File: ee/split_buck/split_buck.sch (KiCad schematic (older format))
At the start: 13 parts, among them J1 Conn_01x08, J3 Conn_01x03, Q1 DMP2160U

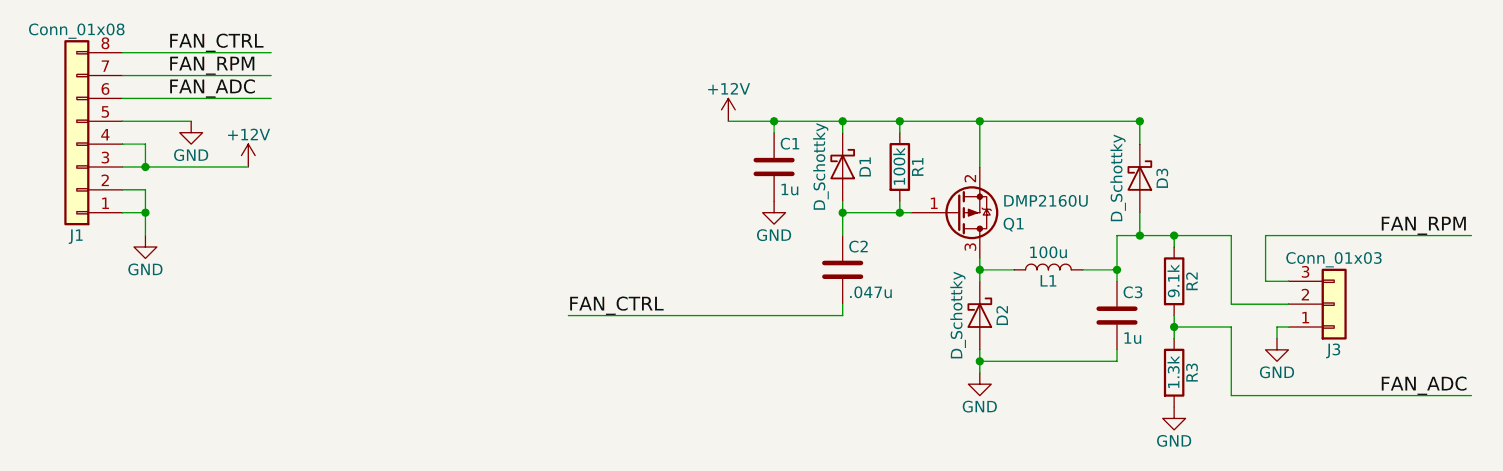
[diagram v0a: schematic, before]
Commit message: Update split_buck design
- switched D1 to zener to protect FET Vgs
- increased input/output caps from 1u to 10u (0603 -> 0805)
- rotated fan header 30degrees to enable multiple channels
- added net names
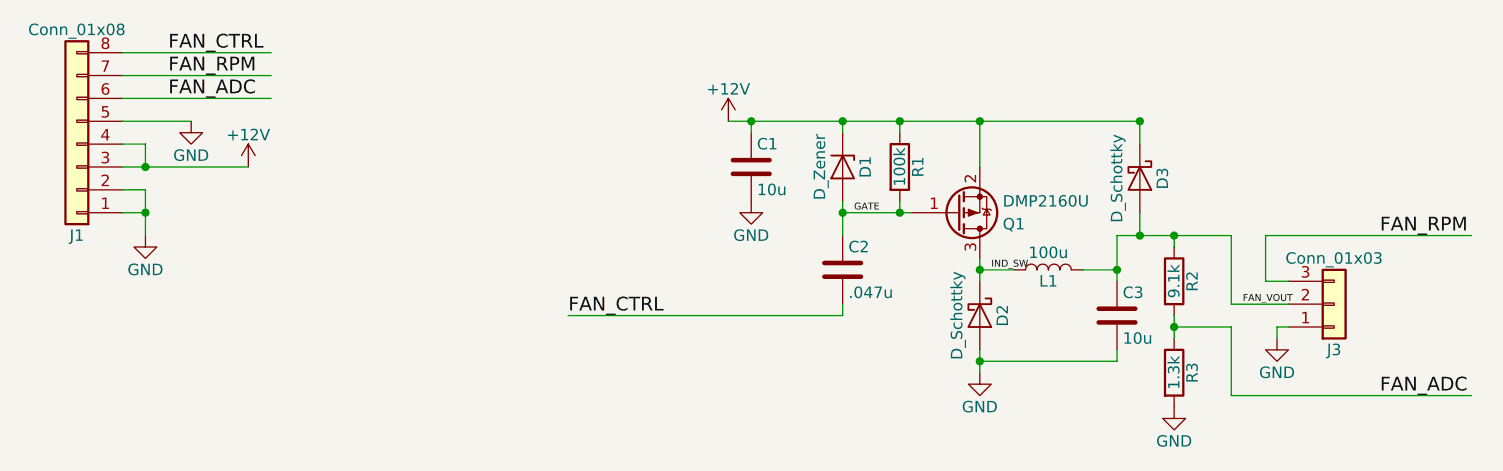
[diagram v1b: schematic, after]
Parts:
- removed D1: D_Schottky, Diodes_SMD:D_SOD-123, symbol D_Schottky
- added D1: D_Zener, Diodes_SMD:D_SOD-123, symbol D_Zener
- C1, C3: value 1u -> 10u; footprint Capacitors_SMD:C_0603_HandSoldering -> Capacitors_SMD:C_0805_HandSoldering
- L1: footprint Inductors_THT:L_Axial_L9.5mm_D4.0mm_P15.24mm_Horizontal_Fastron_SMCC -> Inductors_THT:L_Axial_L7.0mm_D3.3mm_P10.16mm_Horizontal_Fastron_MICC
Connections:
- net labels added: FAN_VOUT, GATE, IND_SW
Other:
- moved on the sheet: C1
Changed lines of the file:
@@
 LIBS:contrib
 LIBS:valves
+LIBS:joystick
 LIBS:stm32
 LIBS:w_connectors
-LIBS:joystick
-LIBS:vent_fan-cache
+LIBS:split_buck-cache
 EELAYER 25 0
 EELAYER END
@@
 F 0 "L1" V 5450 3400 50  0000 C CNN
 F 1 "100u" V 5575 3400 50  0000 C CNN
-F 2 "Inductors_THT:L_Axial_L9.5mm_D4.0mm_P15.24mm_Horizontal_Fastron_SMCC" H 5500 3400 50  0001 C CNN
+F 2 "Inductors_THT:L_Axial_L7.0mm_D3.3mm_P10.16mm_Horizontal_Fastron_MICC" H 5500 3400 50  0001 C CNN
 F 3 "" H 5500 3400 50  0001 C CNN
 	1    5500 3400
 	0    1    -1   0
-$EndComp
-$Comp
-L D_Schottky D1
-U 1 1 5AA40D58
-P 4600 2950
-F 0 "D1" H 4600 3050 50  0000 C CNN
-F 1 "D_Schottky" H 4600 2850 50  0000 C CNN
-F 2 "Diodes_SMD:D_SOD-123" H 4600 2950 50  0001 C CNN
-F 3 "" H 4600 2950 50  0001 C CNN
-	1    4600 2950
-	0    1    1    0
 $EndComp
 $Comp
@@
 L C C1
 U 1 1 5AA40F47
-P 4300 2950
-F 0 "C1" H 4325 3050 50  0000 L CNN
-F 1 "1u" H 4325 2850 50  0000 L CNN
-F 2 "Capacitors_SMD:C_0603_HandSoldering" H 4338 2800 50  0001 C CNN
-F 3 "" H 4300 2950 50  0001 C CNN
-	1    4300 2950
+P 4200 2950
+F 0 "C1" H 4225 3050 50  0000 L CNN
+F 1 "10u" H 4225 2850 50  0000 L CNN
+F 2 "Capacitors_SMD:C_0805_HandSoldering" H 4238 2800 50  0001 C CNN
+F 3 "" H 4200 2950 50  0001 C CNN
+	1    4200 2950
 	1    0    0    -1
 $EndComp
@@
 P 5800 3600
 F 0 "C3" H 5825 3700 50  0000 L CNN
-F 1 "1u" H 5825 3500 50  0000 L CNN
-F 2 "Capacitors_SMD:C_0603_HandSoldering" H 5838 3450 50  0001 C CNN
+F 1 "10u" H 5825 3500 50  0000 L CNN
+F 2 "Capacitors_SMD:C_0805_HandSoldering" H 5838 3450 50  0001 C CNN
 F 3 "" H 5800 3600 50  0001 C CNN
 	1    5800 3600
@@
 L GND #PWR03
 U 1 1 5AA416CE
-P 4300 3100
-F 0 "#PWR03" H 4300 2850 50  0001 C CNN
-F 1 "GND" H 4300 2950 50  0000 C CNN
-F 2 "" H 4300 3100 50  0001 C CNN
-F 3 "" H 4300 3100 50  0001 C CNN
-	1    4300 3100
+P 4200 3100
+F 0 "#PWR03" H 4200 2850 50  0001 C CNN
+F 1 "GND" H 4200 2950 50  0000 C CNN
+F 2 "" H 4200 3100 50  0001 C CNN
+F 3 "" H 4200 3100 50  0001 C CNN
+	1    4200 3100
 	1    0    0    -1
 $EndComp
@@
 Connection ~ 4850 3150
 Connection ~ 5200 3800
-Connection ~ 4300 2750
+Connection ~ 4200 2750
 Wire Wire Line
 	4100 2750 5900 2750
@@
 Connection ~ 4600 3150
 Wire Wire Line
-	4300 2750 4300 2800
+	4200 2750 4200 2800
 Wire Wire Line
 	4850 3100 4850 3150
@@
 	1550 2850 1550 2950
 Connection ~ 1550 2950
+$Comp
+L D_Zener D1
+U 1 1 5AAEA835
+P 4600 2950
+F 0 "D1" H 4600 3050 50  0000 C CNN
+F 1 "D_Zener" H 4600 2850 50  0000 C CNN
+F 2 "Diodes_SMD:D_SOD-123" H 4600 2950 50  0001 C CNN
+F 3 "" H 4600 2950 50  0001 C CNN
+	1    4600 2950
+	0    1    1    0
+$EndComp
+Text Label 6350 3550 0    30   ~ 0
+FAN_VOUT
+Text Label 4650 3150 0    30   ~ 0
+GATE
+Text Label 5250 3400 0    30   ~ 0
+IND_SW
 $EndSCHEMATC

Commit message: update layout for carrier with new pin assignments
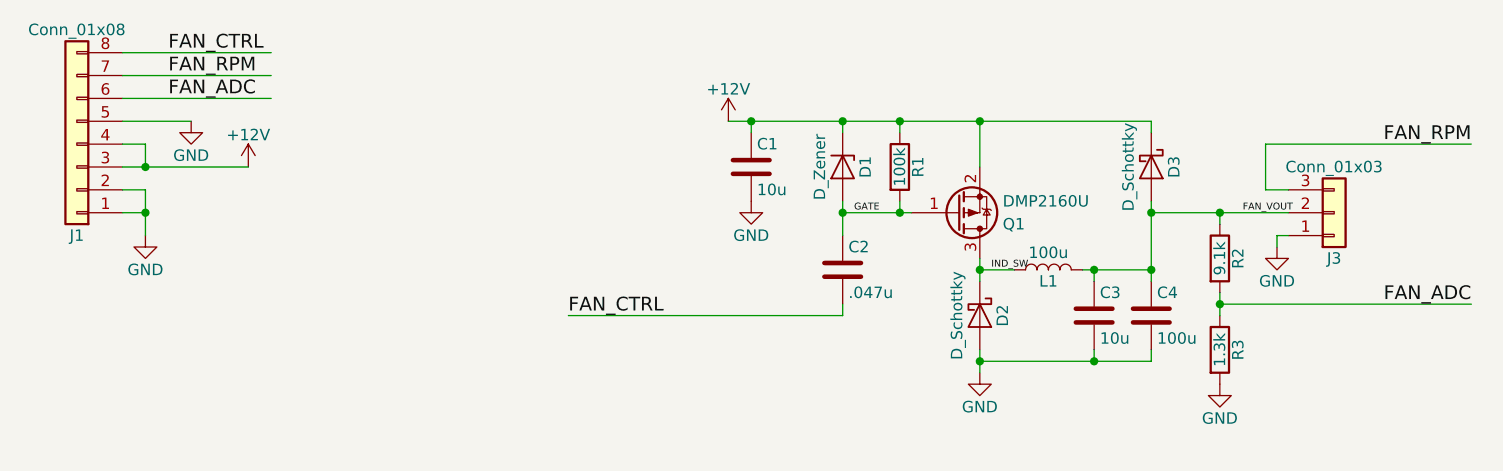
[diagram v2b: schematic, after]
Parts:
- added C4: 100u, Capacitors_THT:CP_Radial_D5.0mm_P2.00mm, symbol C
- J1: footprint custom:Fan_Controller -> custom:Fan_Controller_all
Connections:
- wire segments 42 -> 39
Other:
- moved on the sheet: C3, D3, J3, R2, R3
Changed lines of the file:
@@
 L D_Schottky D3
 U 1 1 5AA40E20
-P 5900 3000
-F 0 "D3" H 5900 3100 50  0000 C CNN
-F 1 "D_Schottky" H 5900 2900 50  0000 C CNN
-F 2 "Diodes_SMD:D_SOD-123" H 5900 3000 50  0001 C CNN
-F 3 "" H 5900 3000 50  0001 C CNN
-	1    5900 3000
+P 5950 2950
+F 0 "D3" H 5950 3050 50  0000 C CNN
+F 1 "D_Schottky" H 5950 2850 50  0000 C CNN
+F 2 "Diodes_SMD:D_SOD-123" H 5950 2950 50  0001 C CNN
+F 3 "" H 5950 2950 50  0001 C CNN
+	1    5950 2950
 	0    1    1    0
 $EndComp
@@
 L C C3
 U 1 1 5AA40FBD
-P 5800 3600
-F 0 "C3" H 5825 3700 50  0000 L CNN
-F 1 "10u" H 5825 3500 50  0000 L CNN
-F 2 "Capacitors_SMD:C_0805_HandSoldering" H 5838 3450 50  0001 C CNN
-F 3 "" H 5800 3600 50  0001 C CNN
-	1    5800 3600
+P 5700 3600
+F 0 "C3" H 5725 3700 50  0000 L CNN
+F 1 "10u" H 5725 3500 50  0000 L CNN
+F 2 "Capacitors_SMD:C_0805_HandSoldering" H 5738 3450 50  0001 C CNN
+F 3 "" H 5700 3600 50  0001 C CNN
+	1    5700 3600
 	1    0    0    -1
 $EndComp
@@
 L Conn_01x03 J3
 U 1 1 5AA4101F
-P 6750 3550
-F 0 "J3" H 6750 3750 50  0000 C CNN
-F 1 "Conn_01x03" H 6750 3350 50  0000 C CNN
-F 2 "Connectors:Fan_Pin_Header_Straight_1x03" H 6750 3550 50  0001 C CNN
-F 3 "" H 6750 3550 50  0001 C CNN
-	1    6750 3550
+P 6750 3150
+F 0 "J3" H 6750 3350 50  0000 C CNN
+F 1 "Conn_01x03" H 6750 2950 50  0000 C CNN
+F 2 "Connectors:Fan_Pin_Header_Straight_1x03" H 6750 3150 50  0001 C CNN
+F 3 "" H 6750 3150 50  0001 C CNN
+	1    6750 3150
 	1    0    0    1
 $EndComp
@@
 Text Label 3400 3600 0    60   ~ 0
 FAN_CTRL
-Text Label 6950 3250 0    60   ~ 0
+Text Label 7350 2850 2    60   ~ 0
 FAN_RPM
 $Comp
 L GND #PWR04
 U 1 1 5AA426F0
-P 6500 3700
-F 0 "#PWR04" H 6500 3450 50  0001 C CNN
-F 1 "GND" H 6500 3550 50  0000 C CNN
-F 2 "" H 6500 3700 50  0001 C CNN
-F 3 "" H 6500 3700 50  0001 C CNN
-	1    6500 3700
+P 6500 3300
+F 0 "#PWR04" H 6500 3050 50  0001 C CNN
+F 1 "GND" H 6500 3150 50  0000 C CNN
+F 2 "" H 6500 3300 50  0001 C CNN
+F 3 "" H 6500 3300 50  0001 C CNN
+	1    6500 3300
 	1    0    0    -1
 $EndComp
@@
 L R R2
 U 1 1 5AA42769
-P 6050 3450
-F 0 "R2" V 6130 3450 50  0000 C CNN
-F 1 "9.1k" V 6050 3450 50  0000 C CNN
-F 2 "Resistors_SMD:R_0603_HandSoldering" V 5980 3450 50  0001 C CNN
-F 3 "" H 6050 3450 50  0001 C CNN
-	1    6050 3450
+P 6250 3350
+F 0 "R2" V 6330 3350 50  0000 C CNN
+F 1 "9.1k" V 6250 3350 50  0000 C CNN
+F 2 "Resistors_SMD:R_0603_HandSoldering" V 6180 3350 50  0001 C CNN
+F 3 "" H 6250 3350 50  0001 C CNN
+	1    6250 3350
 	1    0    0    -1
 $EndComp
@@
 L R R3
 U 1 1 5AA427BE
-P 6050 3850
-F 0 "R3" V 6130 3850 50  0000 C CNN
-F 1 "1.3k" V 6050 3850 50  0000 C CNN
-F 2 "Resistors_SMD:R_0603_HandSoldering" V 5980 3850 50  0001 C CNN
-F 3 "" H 6050 3850 50  0001 C CNN
-	1    6050 3850
+P 6250 3750
+F 0 "R3" V 6330 3750 50  0000 C CNN
+F 1 "1.3k" V 6250 3750 50  0000 C CNN
+F 2 "Resistors_SMD:R_0603_HandSoldering" V 6180 3750 50  0001 C CNN
+F 3 "" H 6250 3750 50  0001 C CNN
+	1    6250 3750
 	1    0    0    -1
 $EndComp
@@
 L GND #PWR05
 U 1 1 5AA42A5B
-P 6050 4000
-F 0 "#PWR05" H 6050 3750 50  0001 C CNN
-F 1 "GND" H 6050 3850 50  0000 C CNN
-F 2 "" H 6050 4000 50  0001 C CNN
-F 3 "" H 6050 4000 50  0001 C CNN
-	1    6050 4000
-	1    0    0    -1
-$EndComp
-Text Label 6950 3950 0    60   ~ 0
+P 6250 3900
+F 0 "#PWR05" H 6250 3650 50  0001 C CNN
+F 1 "GND" H 6250 3750 50  0000 C CNN
+F 2 "" H 6250 3900 50  0001 C CNN
+F 3 "" H 6250 3900 50  0001 C CNN
+	1    6250 3900
+	1    0    0    -1
+$EndComp
+Text Label 7350 3550 2    60   ~ 0
 FAN_ADC
 Connection ~ 4600 2750
@@
 Connection ~ 4200 2750
 Wire Wire Line
-	4100 2750 5900 2750
+	4100 2750 5950 2750
 Connection ~ 5200 2750
 Wire Wire Line
-	6450 3450 6550 3450
-Wire Wire Line
-	6450 3250 7350 3250
-Wire Wire Line
-	6500 3700 6500 3650
-Wire Wire Line
-	6500 3650 6550 3650
+	6450 3050 6550 3050
+Wire Wire Line
+	6450 2850 7350 2850
+Wire Wire Line
+	6500 3300 6500 3250
+Wire Wire Line
+	6500 3250 6550 3250
 Connection ~ 4600 3150
 Wire Wire Line
@@
 Connection ~ 5200 3400
 Wire Wire Line
-	5650 3400 5800 3400
-Wire Wire Line
-	5800 3250 5800 3450
-Connection ~ 5800 3400
+	5650 3400 5950 3400
 Wire Wire Line
 	5200 3750 5200 3850
 Wire Wire Line
-	5800 3750 5800 3800
-Wire Wire Line
-	5800 3800 5200 3800
-Wire Wire Line
-	5900 2750 5900 2850
-Connection ~ 5900 2750
-Wire Wire Line
-	6300 3250 6300 3550
-Wire Wire Line
-	6300 3550 6550 3550
-Wire Wire Line
-	5800 3250 6300 3250
-Wire Wire Line
-	5900 3250 5900 3150
-Connection ~ 5900 3250
-Wire Wire Line
-	6050 3300 6050 3250
-Connection ~ 6050 3250
-Wire Wire Line
-	6050 3600 6050 3700
-Wire Wire Line
-	6050 3650 6300 3650
-Wire Wire Line
-	6300 3650 6300 3950
-Wire Wire Line
-	6300 3950 7350 3950
-Connection ~ 6050 3650
+	5200 3800 5950 3800
+Wire Wire Line
+	6250 3200 6250 3150
+Connection ~ 6250 3150
+Wire Wire Line
+	6250 3500 6250 3600
+Connection ~ 6250 3550
 Wire Wire Line
 	4600 3600 4600 3550
@@
 	1450 2450 2100 2450
 Wire Wire Line
-	6450 3250 6450 3450
+	6450 2850 6450 3050
 Wire Wire Line
 	4600 3600 3400 3600
@@
 F 0 "J1" H 1250 3250 50  0000 C CNN
 F 1 "Conn_01x08" H 1250 2350 50  0000 C CNN
-F 2 "custom:Fan_Controller" H 1250 2850 50  0001 C CNN
+F 2 "custom:Fan_Controller_all" H 1250 2850 50  0001 C CNN
 F 3 "" H 1250 2850 50  0001 C CNN
 	1    1250 2850
@@
 	0    1    1    0
 $EndComp
-Text Label 6350 3550 0    30   ~ 0
+Text Label 6350 3150 0    30   ~ 0
 FAN_VOUT
 Text Label 4650 3150 0    30   ~ 0
@@
 Text Label 5250 3400 0    30   ~ 0
 IND_SW
+$Comp
+L C C4
+U 1 1 5AAF1587
+P 5950 3600
+F 0 "C4" H 5975 3700 50  0000 L CNN
+F 1 "100u" H 5975 3500 50  0000 L CNN
+F 2 "Capacitors_THT:CP_Radial_D5.0mm_P2.00mm" H 5988 3450 50  0001 C CNN
+F 3 "" H 5950 3600 50  0001 C CNN
+	1    5950 3600
+	1    0    0    -1
+$EndComp
+Wire Wire Line
+	5700 3450 5700 3400
+Connection ~ 5700 3400
+Wire Wire Line
+	5700 3750 5700 3800
+Connection ~ 5700 3800
+Wire Wire Line
+	5950 3800 5950 3750
+Wire Wire Line
+	5950 3100 5950 3450
+Connection ~ 5950 3400
+Wire Wire Line
+	5950 3150 6550 3150
+Connection ~ 5950 3150
+Wire Wire Line
+	5950 2750 5950 2800
+Wire Wire Line
+	6250 3550 7350 3550
 $EndSCHEMATC
